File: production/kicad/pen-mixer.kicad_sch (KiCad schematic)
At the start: 28 parts, among them J1 USB-C 16P, J2 BAT, U1 ISP1807-LR, U2 LSM6DS3TR-C, U3 MCP73831T-2ACI/OT, U4 TPS7A0533PDBV

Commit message: battery pads at tip
Claude-Session: https://claude.ai/code/session_01RCYT2QSY7BVZDeTyE9KrC4
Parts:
- J2: footprint pen-mixer:CONN-SMD_P2.00_S2B-PH-SM4-TB-LF-SN -> pen-mixer:SolderPad_1.2x2.0mm; BOM Comments mates JST PH 2.0 battery plug -> bare solder pads - battery wires solder here, no part to or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; LCSC C295747 -> (none); MPN S2B-PH-SM4-TB(LF)(SN) -> (none); Manufacturer JST -> (none)
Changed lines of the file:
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@@
 			)
 		)
-		(property "Footprint" "pen-mixer:CONN-SMD_P2.00_S2B-PH-SM4-TB-LF-SN"
+		(property "Footprint" "pen-mixer:SolderPad_1.2x2.0mm"
 			(at 74.93 92.71 0)
 			(hide yes)
@@
 			)
 		)
-		(property "BOM Comments" "mates JST PH 2.0 battery plug" (at 0 0 0)
+		(property "BOM Comments" "bare solder pads - battery wires solder here, no part to order" (at 0 0 0)
 			(effects
 				(font
@@
 			)
 		)
-		(property "LCSC" "C295747" (at 0 0 0)
+		(property "LCSC" "" (at 0 0 0)
 			(effects
 				(font
@@
 			)
 		)
-		(property "Manufacturer" "JST" (at 0 0 0)
+		(property "Manufacturer" "" (at 0 0 0)
 			(effects
 				(font
@@
 			)
 		)
-		(property "MPN" "S2B-PH-SM4-TB(LF)(SN)" (at 0 0 0)
+		(property "MPN" "" (at 0 0 0)
 			(effects
 				(font

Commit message: add v21 hardware
Claude-Session: https://claude.ai/code/session_01RCYT2QSY7BVZDeTyE9KrC4
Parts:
- added C11: 100n, Capacitor_SMD:C_0402_1005Metric, symbol Device:C
- added LED1, LED2: XL-1010RGBC, pen-mixer:LED-SMD_4P-L1.0-W1.0-TL_XL-1010RGBC-WS2812B, symbol v21:XL-1010RGBC
- added SW1: EVQP7C01P, pen-mixer:SW-SMD_EVQP7C01P, symbol v21:EVQP7C01P
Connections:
- net GND: now also C11.2, LED1.3 (GND), LED2.3 (GND), SW1.2
- net VBAT: now also C11.1, LED1.2 (VDD), LED2.2 (VDD)
- net LED_DATA: now reaches U1.15 (P0.20)
- net LED_DATA: now also LED1.4 (DIN)
- net BTN: now reaches U1.27 (P0.17)
- net BTN: now also SW1.1
- new net LED_LINK: LED1.1 (DOUT), LED2.4 (DIN)
- no-connect marks 60 -> 61
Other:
- note added: "USER INTERFACE (v2.1)"
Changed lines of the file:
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@@
 	)
 	(no_connect
-		(at 237.49 107.95)
-	)
-	(no_connect
 		(at 208.28 33.02)
 	)
@@
 	)
 	(no_connect
-		(at 229.87 107.95)
-	)
-	(no_connect
 		(at 114.3 105.41)
 	)
@@
 		(color 0 0 0 0)
 	)
+	(symbol
+		(lib_id "v21:XL-1010RGBC")
+		(at 155 175 0)
+		(unit 1)
+		(body_style 1)
+		(exclude_from_sim no)
+		(in_bom yes)
+		(on_board yes)
+		(dnp no)
+		(property "Reference" "LED1" (at 155 167 0)  (effects (font (size 1.27 1.27))))
+		(property "Value" "XL-1010RGBC" (at 155 183 0)  (effects (font (size 1.27 1.27))))
+		(property "Footprint" "pen-mixer:LED-SMD_4P-L1.0-W1.0-TL_XL-1010RGBC-WS2812B" (at 155 175 0) (hide yes) (effects (font (size 1.27 1.27))))
+		(property "Datasheet" "" (at 155 175 0) (hide yes) (effects (font (size 1.27 1.27))))
+		(property "MPN" "XL-1010RGBC-2812B" (at 155 175 0) (hide yes) (effects (font (size 1.27 1.27))))
+		(property "Manufacturer" "XINGLIGHT" (at 155 175 0) (hide yes) (effects (font (size 1.27 1.27))))
+		(property "LCSC" "C5349953" (at 155 175 0) (hide yes) (effects (font (size 1.27 1.27))))
+		(property "BOM Comments" "battery level indicator" (at 155 175 0) (hide yes) (effects (font (size 1.27 1.27))))
+		(instances (project "pen-mixer" (path "/0684e67f-dde5-4049-a068-2c0d069dd8c7" (reference "LED1") (unit 1))))
+	)
+	(symbol
+		(lib_id "v21:XL-1010RGBC")
+		(at 185 175 0)
+		(unit 1)
+		(body_style 1)
+		(exclude_from_sim no)
+		(in_bom yes)
+		(on_board yes)
+		(dnp no)
+		(property "Reference" "LED2" (at 185 167 0)  (effects (font (size 1.27 1.27))))
+		(property "Value" "XL-1010RGBC" (at 185 183 0)  (effects (font (size 1.27 1.27))))
+		(property "Footprint" "pen-mixer:LED-SMD_4P-L1.0-W1.0-TL_XL-1010RGBC-WS2812B" (at 185 175 0) (hide yes) (effects (font (size 1.27 1.27))))
+		(property "Datasheet" "" (at 185 175 0) (hide yes) (effects (font (size 1.27 1.27))))
+		(property "MPN" "XL-1010RGBC-2812B" (at 185 175 0) (hide yes) (effects (font (size 1.27 1.27))))
+		(property "Manufacturer" "XINGLIGHT" (at 185 175 0) (hide yes) (effects (font (size 1.27 1.27))))
+		(property "LCSC" "C5349953" (at 185 175 0) (hide yes) (effects (font (size 1.27 1.27))))
+		(property "BOM Comments" "bluetooth status indicator" (at 185 175 0) (hide yes) (effects (font (size 1.27 1.27))))
+		(instances (project "pen-mixer" (path "/0684e67f-dde5-4049-a068-2c0d069dd8c7" (reference "LED2") (unit 1))))
+	)
+	(symbol
+		(lib_id "v21:EVQP7C01P")
+		(at 160 190 0)
+		(unit 1)
+		(body_style 1)
+		(exclude_from_sim no)
+		(in_bom yes)
+		(on_board yes)
+		(dnp no)
+		(property "Reference" "SW1" (at 160 182 0)  (effects (font (size 1.27 1.27))))
+		(property "Value" "EVQP7C01P" (at 160 198 0)  (effects (font (size 1.27 1.27))))
+		(property "Footprint" "pen-mixer:SW-SMD_EVQP7C01P" (at 160 190 0) (hide yes) (effects (font (size 1.27 1.27))))
+		(property "Datasheet" "" (at 160 190 0) (hide yes) (effects (font (size 1.27 1.27))))
+		(property "MPN" "EVQP7C01P" (at 160 190 0) (hide yes) (effects (font (size 1.27 1.27))))
+		(property "Manufacturer" "PANASONIC" (at 160 190 0) (hide yes) (effects (font (size 1.27 1.27))))
+		(property "LCSC" "C388883" (at 160 190 0) (hide yes) (effects (font (size 1.27 1.27))))
+		(property "BOM Comments" "power and pairing button, side actuated" (at 160 190 0) (hide yes) (effects (font (size 1.27 1.27))))
+		(instances (project "pen-mixer" (path "/0684e67f-dde5-4049-a068-2c0d069dd8c7" (reference "SW1") (unit 1))))
+	)
+	(symbol
+		(lib_id "Device:C")
+		(at 205 186 0)
+		(unit 1)
+		(body_style 1)
+		(exclude_from_sim no)
+		(in_bom yes)
+		(on_board yes)
+		(dnp no)
+		(property "Reference" "C11" (at 205 178 0)  (effects (font (size 1.27 1.27))))
+		(property "Value" "100n" (at 205 194 0)  (effects (font (size 1.27 1.27))))
+		(property "Footprint" "Capacitor_SMD:C_0402_1005Metric" (at 205 186 0) (hide yes) (effects (font (size 1.27 1.27))))
+		(property "Datasheet" "" (at 205 186 0) (hide yes) (effects (font (size 1.27 1.27))))
+		(property "MPN" "CL05B104KO5NNNC" (at 205 186 0) (hide yes) (effects (font (size 1.27 1.27))))
+		(property "Manufacturer" "Samsung Electro-Mechanics" (at 205 186 0) (hide yes) (effects (font (size 1.27 1.27))))
+		(property "LCSC" "C1525" (at 205 186 0) (hide yes) (effects (font (size 1.27 1.27))))
+		(instances (project "pen-mixer" (path "/0684e67f-dde5-4049-a068-2c0d069dd8c7" (reference "C11") (unit 1))))
+	)
+	(global_label "LED_LINK"
+		(shape bidirectional)
+		(at 144.84 173.73 180)
+		(fields_autoplaced yes)
+		(effects (font (size 1.27 1.27)) (justify right))
+		(property "Intersheetrefs" "${INTERSHEET_REFS}" (at 144.84 173.73 0) (hide yes) (show_name no) (do_not_autoplace no) (effects (font (size 1.27 1.27))))
+	)
+	(global_label "GND"
+		(shape bidirectional)
+		(at 144.84 176.27 180)
+		(fields_autoplaced yes)
+		(effects (font (size 1.27 1.27)) (justify right))
+		(property "Intersheetrefs" "${INTERSHEET_REFS}" (at 144.84 176.27 0) (hide yes) (show_name no) (do_not_autoplace no) (effects (font (size 1.27 1.27))))
+	)
+	(global_label "VBAT"
+		(shape bidirectional)
+		(at 165.16 173.73 0)
+		(fields_autoplaced yes)
+		(effects (font (size 1.27 1.27)) (justify left))
+		(property "Intersheetrefs" "${INTERSHEET_REFS}" (at 165.16 173.73 0) (hide yes) (show_name no) (do_not_autoplace no) (effects (font (size 1.27 1.27))))
+	)
+	(global_label "LED_DATA"
+		(shape bidirectional)
+		(at 165.16 176.27 0)
+		(fields_autoplaced yes)
+		(effects (font (size 1.27 1.27)) (justify left))
+		(property "Intersheetrefs" "${INTERSHEET_REFS}" (at 165.16 176.27 0) (hide yes) (show_name no) (do_not_autoplace no) (effects (font (size 1.27 1.27))))
+	)
+	(no_connect
+		(at 174.84 173.73)
+	)
+	(global_label "GND"
+		(shape bidirectional)
+		(at 174.84 176.27 180)
+		(fields_autoplaced yes)
+		(effects (font (size 1.27 1.27)) (justify right))
+		(property "Intersheetrefs" "${INTERSHEET_REFS}" (at 174.84 176.27 0) (hide yes) (show_name no) (do_not_autoplace no) (effects (font (size 1.27 1.27))))
+	)
+	(global_label "VBAT"
+		(shape bidirectional)
+		(at 195.16 173.73 0)
+		(fields_autoplaced yes)
+		(effects (font (size 1.27 1.27)) (justify left))
+		(property "Intersheetrefs" "${INTERSHEET_REFS}" (at 195.16 173.73 0) (hide yes) (show_name no) (do_not_autoplace no) (effects (font (size 1.27 1.27))))
+	)
+	(global_label "LED_LINK"
+		(shape bidirectional)
+		(at 195.16 176.27 0)
+		(fields_autoplaced yes)
+		(effects (font (size 1.27 1.27)) (justify left))
+		(property "Intersheetrefs" "${INTERSHEET_REFS}" (at 195.16 176.27 0) (hide yes) (show_name no) (do_not_autoplace no) (effects (font (size 1.27 1.27))))
+	)
+	(global_label "BTN"
+		(shape bidirectional)
+		(at 152.38 188.73 180)
+		(fields_autoplaced yes)
+		(effects (font (size 1.27 1.27)) (justify right))
+		(property "Intersheetrefs" "${INTERSHEET_REFS}" (at 152.38 188.73 0) (hide yes) (show_name no) (do_not_autoplace no) (effects (font (size 1.27 1.27))))
+	)
+	(global_label "GND"
+		(shape bidirectional)
+		(at 152.38 193.81 180)
+		(fields_autoplaced yes)
+		(effects (font (size 1.27 1.27)) (justify right))
+		(property "Intersheetrefs" "${INTERSHEET_REFS}" (at 152.38 193.81 0) (hide yes) (show_name no) (do_not_autoplace no) (effects (font (size 1.27 1.27))))
+	)
+	(no_connect
+		(at 167.62 188.73)
+	)
+	(no_connect
+		(at 167.62 193.81)
+	)
+	(global_label "VBAT"
+		(shape bidirectional)
+		(at 205 182.19 90)
+		(fields_autoplaced yes)
+		(effects (font (size 1.27 1.27)) (justify left))
+		(property "Intersheetrefs" "${INTERSHEET_REFS}" (at 205 182.19 0) (hide yes) (show_name no) (do_not_autoplace no) (effects (font (size 1.27 1.27))))
+	)
+	(global_label "GND"
+		(shape bidirectional)
+		(at 205 189.81 270)
+		(fields_autoplaced yes)
+		(effects (font (size 1.27 1.27)) (justify left))
+		(property "Intersheetrefs" "${INTERSHEET_REFS}" (at 205 189.81 0) (hide yes) (show_name no) (do_not_autoplace no) (effects (font (size 1.27 1.27))))
+	)
+	(global_label "LED_DATA"
+		(shape bidirectional)
+		(at 237.49 107.95 270)
+		(fields_autoplaced yes)
+		(effects (font (size 1.27 1.27)) (justify left))
+		(property "Intersheetrefs" "${INTERSHEET_REFS}" (at 237.49 107.95 0) (hide yes) (show_name no) (do_not_autoplace no) (effects (font (size 1.27 1.27))))
+	)
+	(global_label "BTN"
+		(shape bidirectional)
+		(at 229.87 107.95 270)
+		(fields_autoplaced yes)
+		(effects (font (size 1.27 1.27)) (justify left))
+		(property "Intersheetrefs" "${INTERSHEET_REFS}" (at 229.87 107.95 0) (hide yes) (show_name no) (do_not_autoplace no) (effects (font (size 1.27 1.27))))
+	)
+	(rectangle
+		(start 140 165)
+		(end 215 198)
+		(stroke (width 0.1524) (type dash) (color 0 0 194 1))
+		(fill (type none))
+	)
+	(text "USER INTERFACE (v2.1)"
+		(exclude_from_sim no)
+		(at 141 163.5 0)
+		(effects (font (size 2 2) (bold yes) (color 0 0 194 1)) (justify left bottom))
+	)
 	(sheet_instances

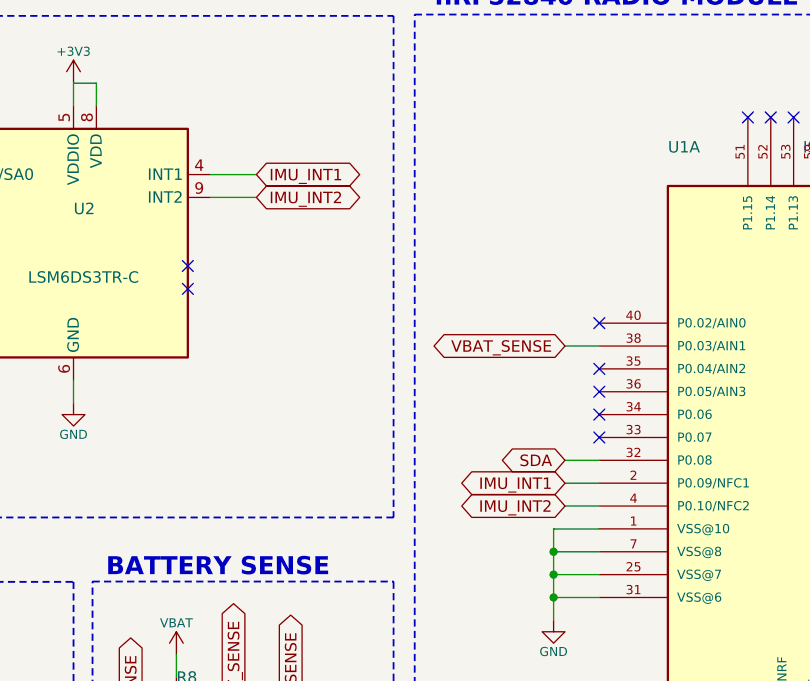
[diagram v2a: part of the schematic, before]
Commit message: free nfc pins from imu
Disconnect IMU_INT1/INT2 from U1 P0.09/P0.10 (NFC1/NFC2) so the NFC
antenna can use them; the firmware polls the IMU and never used the
interrupts. Schematic: 4 wires and 4 labels removed, no-connect flags on
U1 pins 2, 4 and U2 INT1, INT2. PCB: 24 tracks and vias and 4 pad nets
removed. DRC 0 violations, 0 unconnected; ERC unchanged; netlist matches
reference-nets.json after the four intended removals.

Claude-Session: https://claude.ai/code/session_01Q1V828NK1ouT6YXKEbiFUx
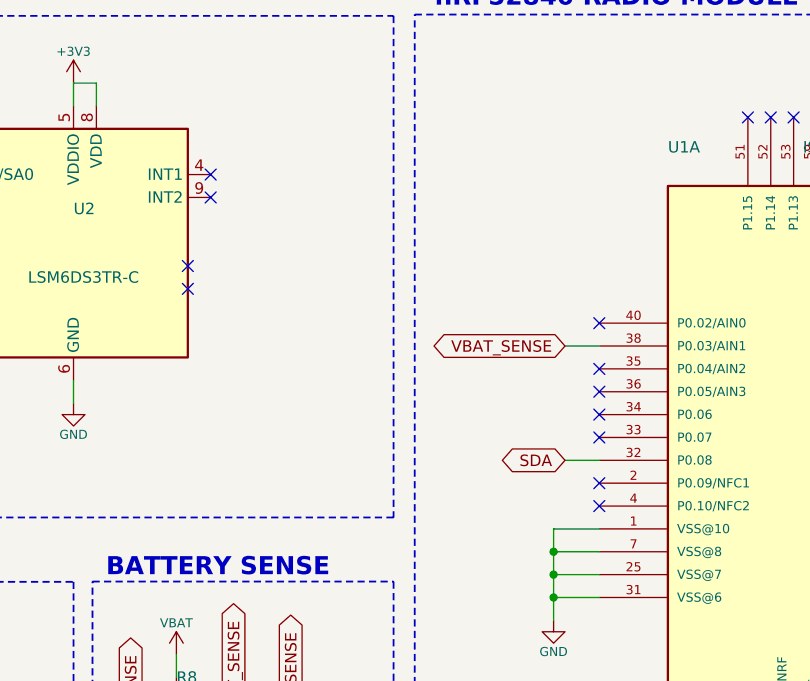
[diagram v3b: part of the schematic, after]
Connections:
- net IMU_INT1: no longer names the net of U1.2 (P0.09/NFC1)
- net IMU_INT1: no longer U2.4 (INT1)
- net IMU_INT2: no longer names the net of U1.4 (P0.10/NFC2)
- net IMU_INT2: no longer U2.9 (INT2)
- no-connect marks 61 -> 65
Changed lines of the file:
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@@
 	(wire
 		(pts
-			(xy 148.59 41.91) (xy 153.67 41.91)
-		)
-		(stroke
-			(width 0.1524)
-			(type solid)
-			(color 0 132 0 1)
-		)
-	)
-	(wire
-		(pts
 			(xy 20.32 105.41) (xy 26.67 105.41)
 		)
@@
 	(wire
 		(pts
-			(xy 148.59 39.37) (xy 153.67 39.37)
-		)
-		(stroke
-			(width 0.1524)
-			(type solid)
-			(color 0 132 0 1)
-		)
-	)
-	(wire
-		(pts
 			(xy 45.72 50.8) (xy 48.26 50.8)
 		)
@@
 	(wire
 		(pts
-			(xy 191.77 76.2) (xy 187.96 76.2)
-		)
-		(stroke
-			(width 0.1524)
-			(type solid)
-			(color 0 132 0 1)
-		)
-	)
-	(wire
-		(pts
 			(xy 270.51 46.99) (xy 270.51 49.53)
 		)
@@
 	(wire
 		(pts
-			(xy 191.77 73.66) (xy 187.96 73.66)
-		)
-		(stroke
-			(width 0.1524)
-			(type solid)
-			(color 0 132 0 1)
-		)
-	)
-	(wire
-		(pts
 			(xy 133.35 62.23) (xy 133.35 64.77)
 		)
@@
 		)
 	)
-	(global_label "IMU_INT1"
-		(shape bidirectional)
-		(at 187.96 73.66 180)
-		(fields_autoplaced yes)
-		(effects
-			(font
-				(size 1.27 1.27)
-			)
-			(justify right)
-		)
-		(property "Intersheetrefs" "${INTERSHEET_REFS}"
-			(at 187.96 73.66 0)
-			(hide yes)
-			(show_name no)
-			(do_not_autoplace no)
-			(effects
-				(font
-					(size 1.27 1.27)
-				)
-			)
-		)
-	)
-	(global_label "IMU_INT2"
-		(shape bidirectional)
-		(at 153.67 41.91 0)
-		(fields_autoplaced yes)
-		(effects
-			(font
-				(size 1.27 1.27)
-			)
-			(justify left)
-		)
-		(property "Intersheetrefs" "${INTERSHEET_REFS}"
-			(at 153.67 41.91 0)
-			(hide yes)
-			(show_name no)
-			(do_not_autoplace no)
-			(effects
-				(font
-					(size 1.27 1.27)
-				)
-			)
-		)
-	)
-	(global_label "IMU_INT2"
-		(shape bidirectional)
-		(at 187.96 76.2 180)
-		(fields_autoplaced yes)
-		(effects
-			(font
-				(size 1.27 1.27)
-			)
-			(justify right)
-		)
-		(property "Intersheetrefs" "${INTERSHEET_REFS}"
-			(at 187.96 76.2 0)
-			(hide yes)
-			(show_name no)
-			(do_not_autoplace no)
-			(effects
-				(font
-					(size 1.27 1.27)
-				)
-			)
-		)
-	)
 	(global_label "VBAT_SENSE"
 		(shape bidirectional)
@@
 		)
 	)
-	(global_label "IMU_INT1"
-		(shape bidirectional)
-		(at 153.67 39.37 0)
-		(fields_autoplaced yes)
-		(effects
-			(font
-				(size 1.27 1.27)
-			)
-			(justify left)
-		)
-		(property "Intersheetrefs" "${INTERSHEET_REFS}"
-			(at 153.67 39.37 0)
-			(hide yes)
-			(show_name no)
-			(do_not_autoplace no)
-			(effects
-				(font
-					(size 1.27 1.27)
-				)
-			)
-		)
-	)
 	(global_label "USB_DM"
 		(shape bidirectional)
@@
 	)
 	(embedded_fonts no)
+	(no_connect
+		(at 148.59 39.37)
+	)
+	(no_connect
+		(at 148.59 41.91)
+	)
+	(no_connect
+		(at 191.77 73.66)
+	)
+	(no_connect
+		(at 191.77 76.2)
+	)
 )

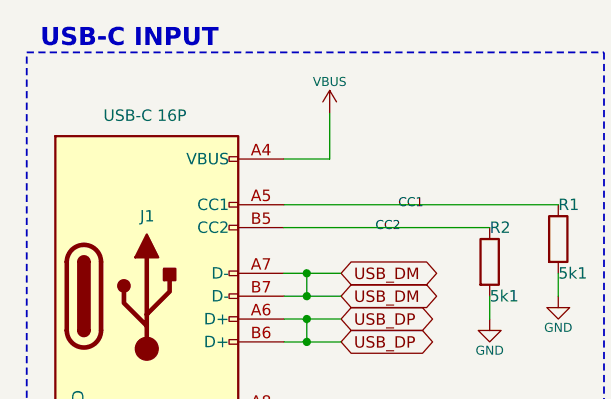
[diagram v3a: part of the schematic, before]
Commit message: add v3 star board
Regular five-point star, 40 mm tip to tip, antenna at the top prong with
its copper keep-out, all v2.1 parts kept. J1 becomes a vertical top-entry
USB-C (G-Switch GT-USB-7055E, C7450622, footprint and 3D model via
easyeda2kicad) so every prong stays identical; schematic netlist is
IDENTICAL to reference-nets.json. Routed with freerouting (0 unrouted),
GND pours on all four layers refilled, DRC 0 errors and 0 unconnected
with only the two accepted label text-thickness warnings, schematic
parity clean. U3 pad 2 connects solid to the pour (no room for two
thermal spokes). Renders in production/output/v3.

Claude-Session: https://claude.ai/code/session_01Q1V828NK1ouT6YXKEbiFUx
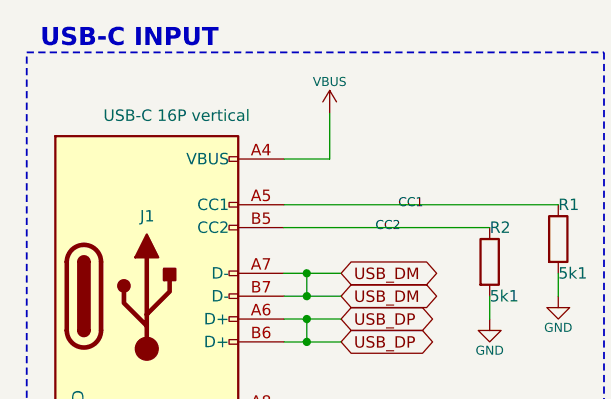
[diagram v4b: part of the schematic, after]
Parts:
- J1: value USB-C 16P -> USB-C 16P vertical; footprint Connector_USB:USB_C_Receptacle_G-Switch_GT-USB-7010ASV -> pen-mixer:USB-C-SMD_GT-USB-7055E; LCSC C2988369 -> C7450622; MPN GT-USB-7010ASV -> GT-USB-7055E
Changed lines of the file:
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@@
 			)
 		)
-		(property "Value" "USB-C 16P"
+		(property "Value" "USB-C 16P vertical"
 			(at 25.654 28.194 0)
 			(show_name no)
@@
 			)
 		)
-		(property "Footprint" "Connector_USB:USB_C_Receptacle_G-Switch_GT-USB-7010ASV"
+		(property "Footprint" "pen-mixer:USB-C-SMD_GT-USB-7055E"
 			(at 30.48 48.26 0)
 			(hide yes)
@@
 			)
 		)
-		(property "LCSC" "C2988369" (at 0 0 0)
+		(property "LCSC" "C7450622" (at 0 0 0)
 			(effects
 				(font
@@
 			)
 		)
-		(property "MPN" "GT-USB-7010ASV" (at 0 0 0)
+		(property "MPN" "GT-USB-7055E" (at 0 0 0)
 			(effects
 				(font

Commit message: revise v3 star board
Flat side-entry USB-C recessed in the bottom notch, power button parallel
to the right arm's edge, LEDs mirrored left and right, test and battery
pads in lines parallel to the leg edges, passives aligned, rerouted with
freerouting (28 vias, was 34). Netlist identical to reference-nets.json;
DRC 0 errors, 0 unconnected.

Claude-Session: https://claude.ai/code/session_01FgTSApPZVavJw8HMjYxhL2
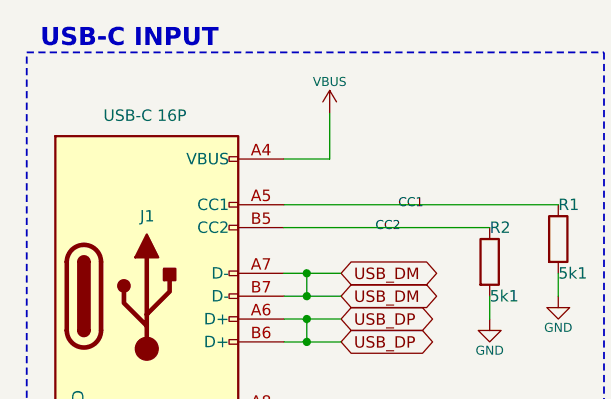
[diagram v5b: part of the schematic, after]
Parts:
- J1: value USB-C 16P vertical -> USB-C 16P; footprint pen-mixer:USB-C-SMD_GT-USB-7055E -> pen-mixer:GT-USB-7010ASV; LCSC C7450622 -> C2988369; MPN GT-USB-7055E -> GT-USB-7010ASV
